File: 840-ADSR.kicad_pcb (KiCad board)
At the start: 2 copper layers, 38 x 106 mm, 83 parts, among them J1 PJ-301B-JACK, J2 PJ-301B-JACK, J3 PJ-301B-JACK, J4 PJ-301B-JACK, J5 PJ-301B, J6 PJ-301B, J7 PJ-301B, P1 CONN_02X05, Q1 DMMT3906W-K4B, Q2 DMMT3904W, Q3 MMBT3904, Q4 MMBT3904, Q5 MMBT3904, SW1 B3F-1050, T1 10K, T2 10K, U1 TL074-, U2 NE555, U3 CD4052, U4 TL072-

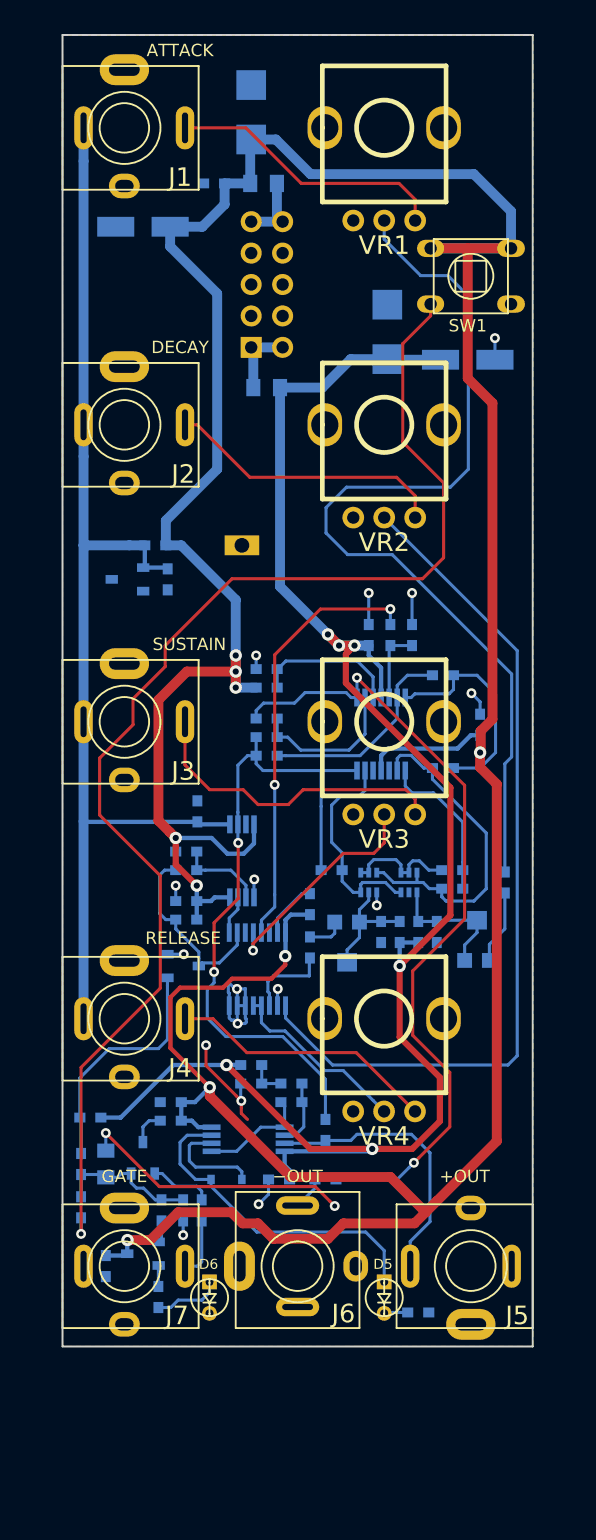
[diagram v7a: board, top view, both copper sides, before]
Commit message: v1.1 in the works. buffered env output to 555 threshold input, changed 10V reference distribution added some notes
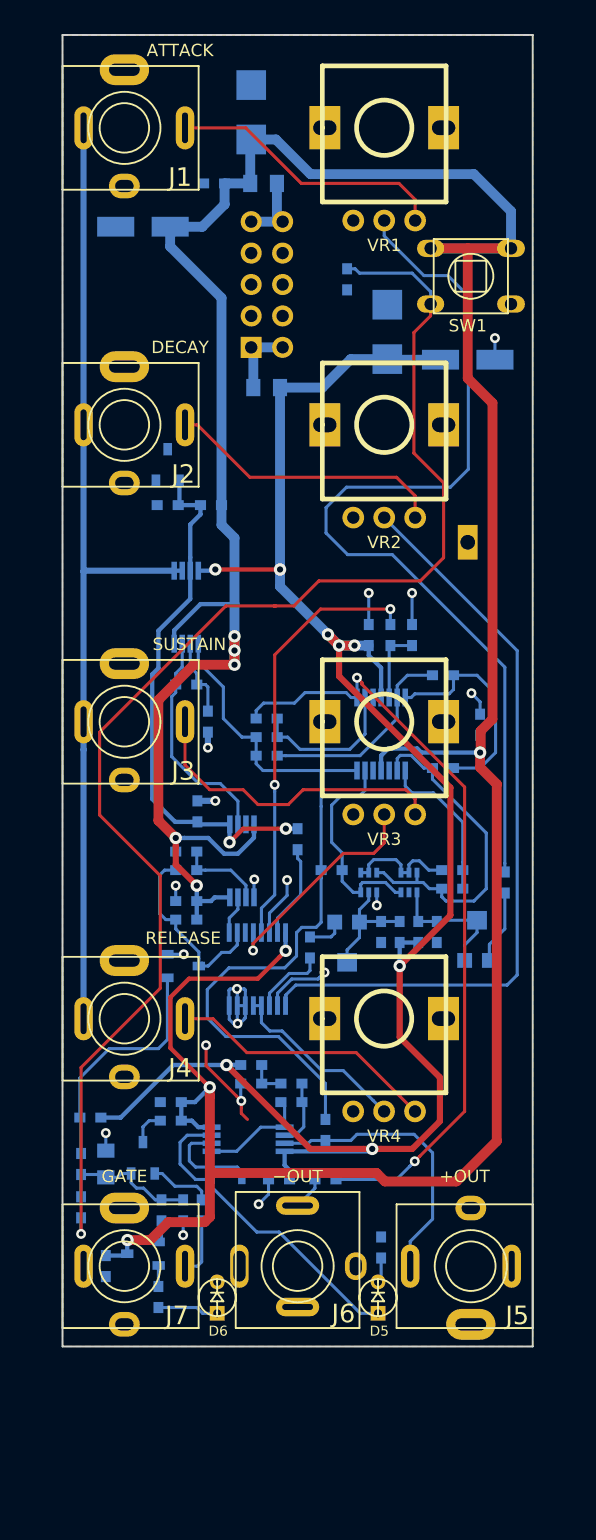
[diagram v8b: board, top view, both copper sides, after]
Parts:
- added R11: 47K, MyModules:SM0603-R-YAGEO, B.Cu at (103.0, 69.5)
- added U5: TL072-, MyModules:TSSOP-8_4.4x3mm_Pitch0.65mm, B.Cu at (90.0, 96.0)
- C8: value 100n** -> 100n
- R1: value 1K -> 220
- R4: value 10K -> 22K
- R6: value 10K -> 1meg
- VR1, VR2, VR3, VR4: footprint MyModules:RD901F-ALPHA-POT-T18 -> MyModules:RD901F-40-ALPHA-POT-T18
- moved TP1 18.3 mm to (112.8, 90.8), turned to 90 degrees
- moved D3 9.80 mm to (88.5, 84.5), turned to 180 degrees
- moved R4 6.62 mm to (90.0, 102.2)
- moved R36 6.05 mm to (105.8, 147.8), turned to 270 degrees
- moved C4 6.00 mm to (88.5, 87.8), turned to 180 degrees
- moved R1 5.55 mm to (92.0, 87.8)
- moved R6 5.49 mm to (91.8, 105.2), turned to 270 degrees
- moved R15 5.34 mm to (99.0, 114.8), turned to 270 degrees
- moved D6 0.62 mm to (92.5, 151.8), turned to 90 degrees
- moved D5 0.50 mm to (105.5, 151.8), turned to 90 degrees
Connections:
- J1 pad 2: +10V -> /POT_REF
- J2 pad 2: +10V -> /POT_REF
- J3 pad 2: +10V -> /POT_REF
- J4 pad 2: +10V -> /POT_REF
- J7 pad 2: Net-(J7-Pad2) -> GND
- R15 pad 1: +12V -> +10V
- R4 pad 1: GND -> Net-(R4-Pad1)
- R6 pad 1: +12V -> Net-(R4-Pad2)
- R6 pad 2: Net-(R4-Pad2) -> GND
- U1 pad 10: Net-(R4-Pad2) -> GND
- U2 pad 6: Net-(C8-Pad1) -> Net-(R4-Pad1)
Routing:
- net /POT_REF: track 0.00 -> 80.0 mm
- net +10V: track 92.8 -> 43.8 mm, vias 0 -> 2
- net +12V: track 315.5 -> 295.9 mm
- net Net-(R4-Pad1): track 0.00 -> 18.2 mm
- net GND: track 63.4 -> 51.9 mm, vias 18 -> 19
- net DECAY: track 69.6 -> 61.7 mm
- net Net-(R11-Pad1): track 104.0 -> 110.9 mm
- net -12V: track 139.8 -> 146.4 mm, vias 6 -> 8
- net Net-(C8-Pad1): track 56.7 -> 62.5 mm, vias 2 -> 0
- net Net-(R4-Pad2): track 11.7 -> 6.45 mm
- net Net-(R15-Pad2): track 4.62 -> 7.58 mm
- net Net-(R30-Pad1): track 65.0 -> 62.5 mm
- net Net-(R21-Pad1): track 7.01 -> 6.05 mm
- net Net-(D4-Pad1): track 26.8 -> 25.9 mm
- net ENV_OUT: track 22.5 -> 23.1 mm
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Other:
- board text added: "r1.1 11/2018"
- board text removed: "r1.0 9/2018"
